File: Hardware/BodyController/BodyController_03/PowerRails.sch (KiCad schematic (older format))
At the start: 44 parts, among them Q10 NX1029X,115, Q11 NX1029X,115, U18 TLV70033DDC, U19 TLV70033DDC, U20 LMR140x0

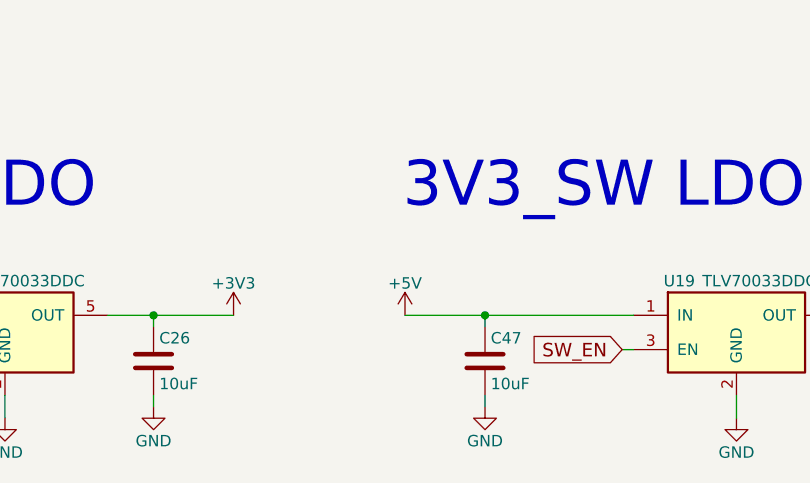
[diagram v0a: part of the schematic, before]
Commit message: Updated layout, cleaned up directory, and modified BOM
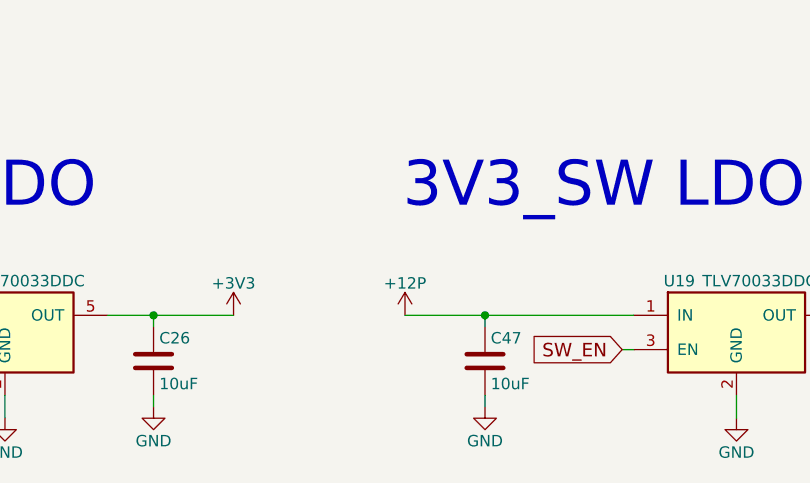
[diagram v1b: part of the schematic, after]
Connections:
- net +12P: now also C47.1, U19.1 (IN)
- net +5V: no longer C47.1, U19.1 (IN)
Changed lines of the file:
@@
 EESchema Schematic File Version 2
+LIBS:BodyController_03-rescue
 LIBS:power
 LIBS:device
@@
 LIBS:contrib
 LIBS:valves
-LIBS:HSD
-LIBS:micros
-LIBS:ICs
-LIBS:Connectors
 LIBS:BodyController_03-cache
 EELAYER 25 0
@@
 F 3 "http://www.ti.com/lit/ds/slvsa00e/slvsa00e.pdf" H 5550 6950 50  0001 C CNN
 	1    5550 6950
-	1    0    0    -1
-$EndComp
-$Comp
-L +5V #PWR0214
-U 1 1 59A6B09C
-P 4100 6900
-F 0 "#PWR0214" H 4100 6750 50  0001 C CNN
-F 1 "+5V" H 4100 7040 50  0000 C CNN
-F 2 "" H 4100 6900 50  0001 C CNN
-F 3 "" H 4100 6900 50  0001 C CNN
-	1    4100 6900
 	1    0    0    -1
 $EndComp
@@
 Connection ~ 3500 4000
 Connection ~ 4850 4900
+$Comp
+L +12P #PWR?
+U 1 1 59ED23A1
+P 4100 6900
+F 0 "#PWR?" H 4100 6750 50  0001 C CNN
+F 1 "+12P" H 4100 7040 50  0000 C CNN
+F 2 "" H 4100 6900 50  0001 C CNN
+F 3 "" H 4100 6900 50  0001 C CNN
+	1    4100 6900
+	1    0    0    -1
+$EndComp
 $EndSCHEMATC

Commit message: started serious layout
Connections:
- net +12P: no longer C47.1, U19.1 (IN)
- net +12V: now also C47.1, U19.1 (IN)
- net 12P_MONITOR renamed 12P_MONITOR_AI

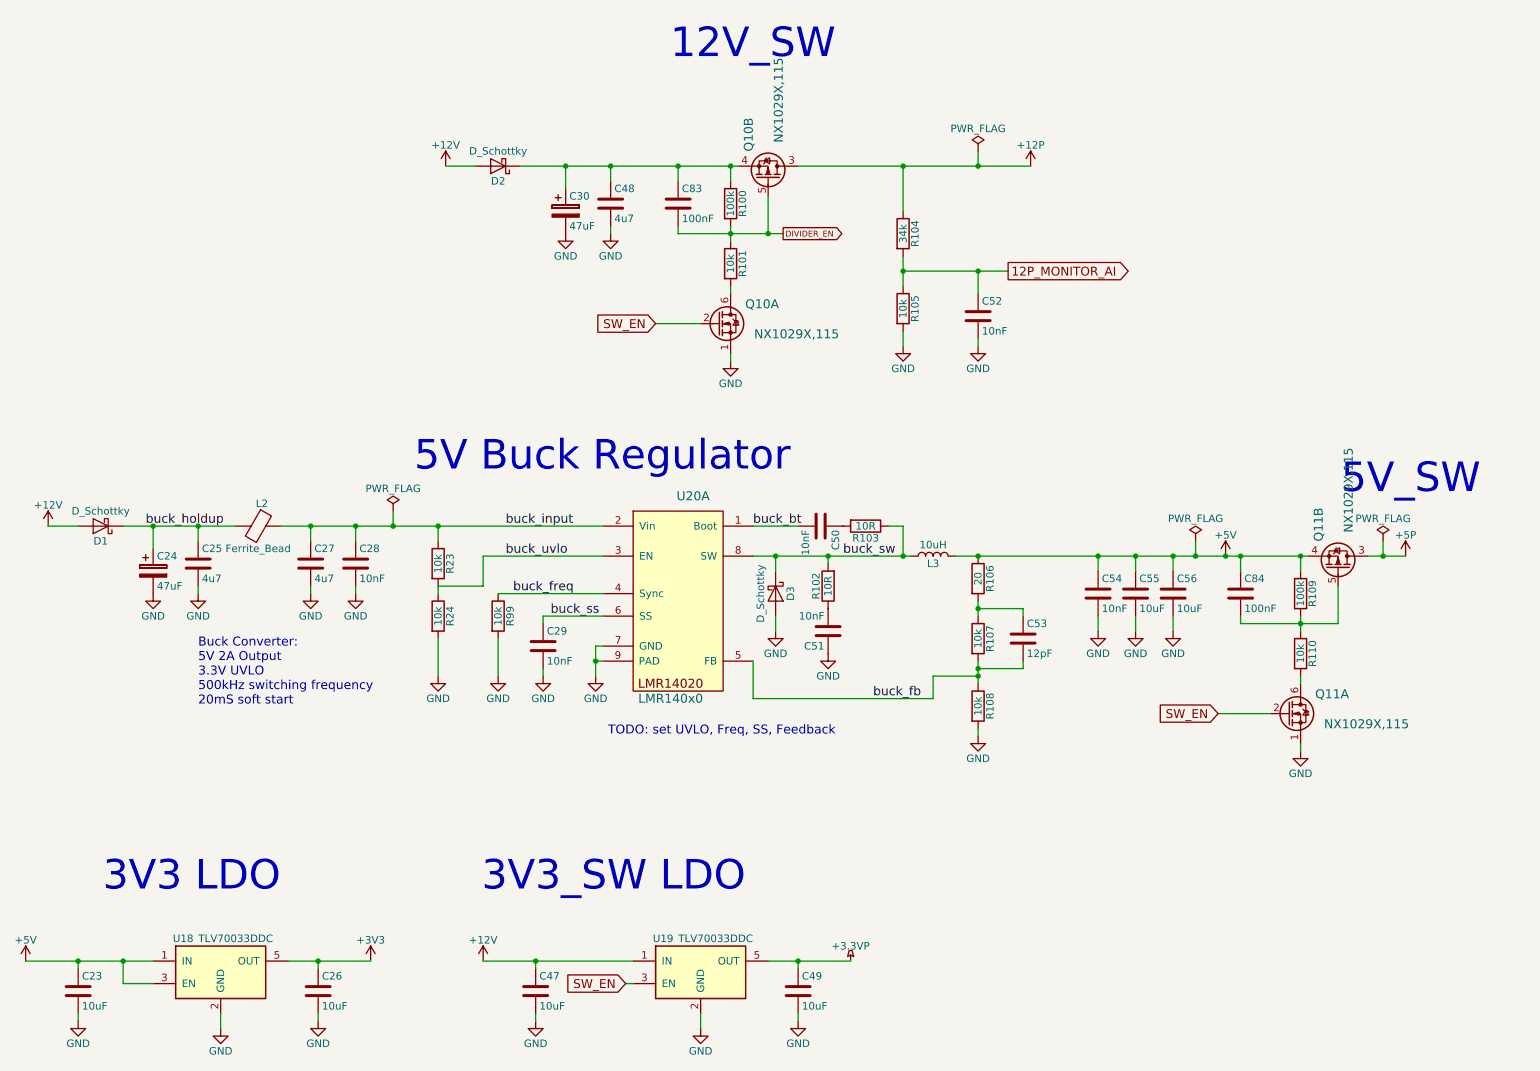
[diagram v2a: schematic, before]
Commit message: Body Controller Layout Done
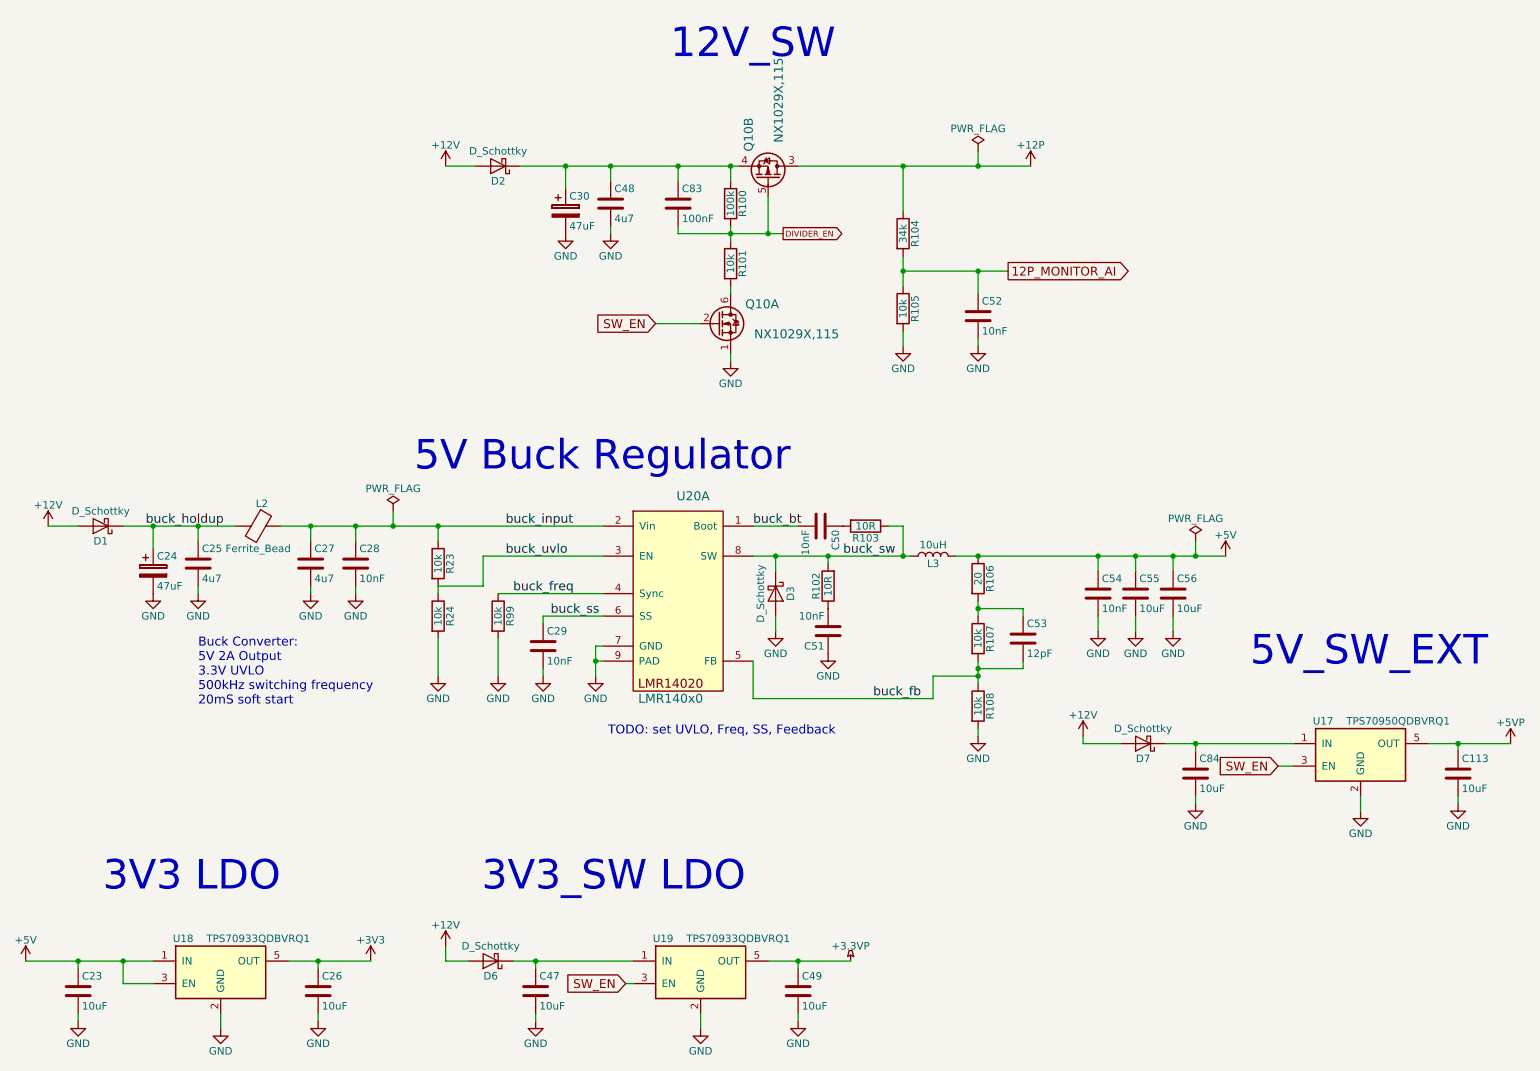
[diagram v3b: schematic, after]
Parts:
- removed Q11: NX1029X,115, TO_SOT_Packages_SMD:SOT-666, symbol NX1029X,115
- removed R109: 100k, Resistors_SMD:R_0603, symbol R
- removed R110: 10k, Resistors_SMD:R_0603, symbol R
- added C113: 10uF, Capacitors_SMD:C_1206, symbol C
- added D6, D7: D_Schottky, Diodes_SMD:D_SOD-123, symbol D_Schottky
- added U17: TPS70950QDBVRQ1, TO_SOT_Packages_SMD:SOT-23-5, symbol TLV70033DDC
- C84: value 100nF -> 10uF; footprint Capacitors_SMD:C_0603 -> Capacitors_SMD:C_1206; PartNumber CGA3E2X7R1H104K080AA -> CGA5L1X7R1E106M160AC
- U18, U19: value TLV70033DDC -> TPS70933QDBVRQ1; PartNumber (none) -> TPS70933QDBVRQ1
- U20: footprint Housings_SOIC:Diodes_PSOP-8 -> Housings_SOIC:HTSOP-8-1EP_3.9x4.9mm_Pitch1.27mm_ThermalVias
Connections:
- net +12V: now also D6.2 (A), D7.2 (A); no longer C47.1, U19.1 (IN)
- net +5V: no longer C84.1
- net GND: now also C84.2, C113.2, U17.2 (GND)
- net SW_EN: now also U17.3 (EN)
- new net: C47.1, D6.1 (K), U19.1 (IN)
- new net: C84.1, D7.1 (K), U17.1 (IN)
- new net +5VP: C113.1, U17.5 (OUT)
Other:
- note added: "5V_SW_EXT"
- note removed: "5V_SW"

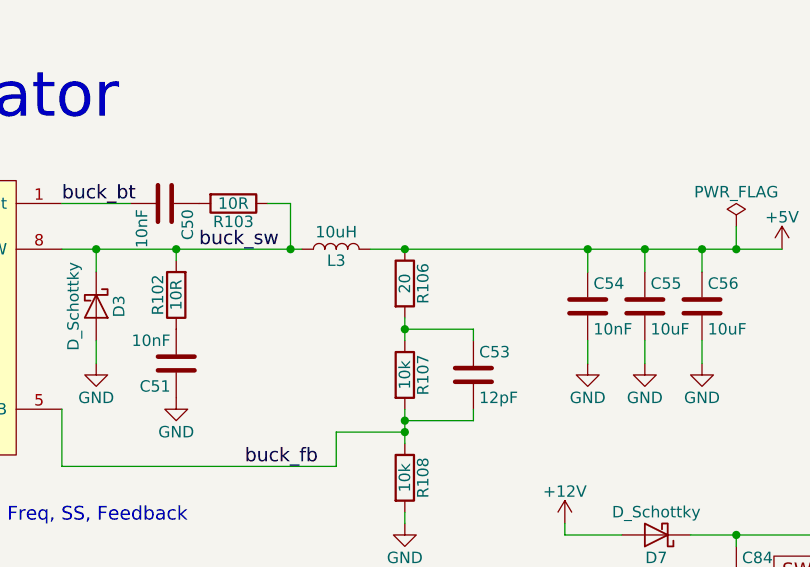
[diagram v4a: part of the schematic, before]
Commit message: Added resistor values via BOM importer. Changed layout file to add large CAN resistors and buffer to 1.65V Reference
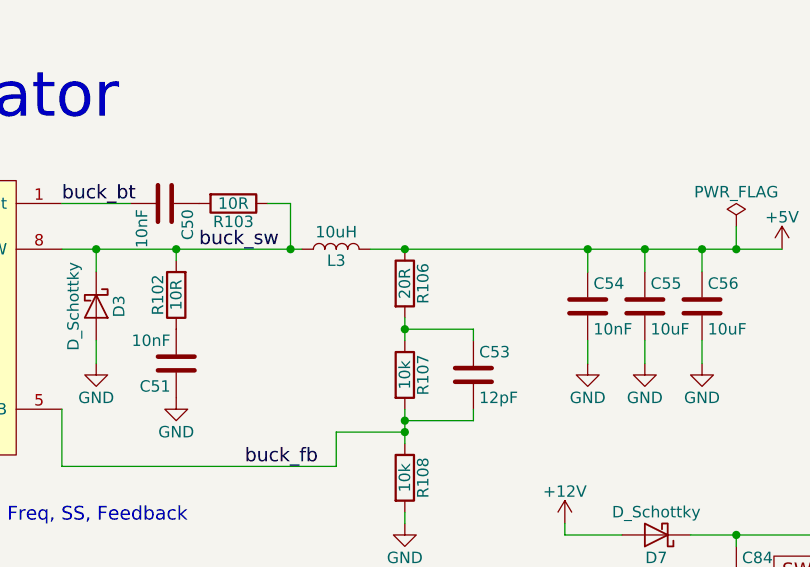
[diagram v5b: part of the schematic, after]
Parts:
- R100: PartNumber (none) -> AC0603FR-07100KL
- R101, R105, R107, R108, R23, R24, R99: PartNumber (none) -> AC0603FR-0710KL
- R102, R103: PartNumber (none) -> AC0603FR-0710RL
- R104: PartNumber (none) -> ERJ-3EKF3402V
- R106: value 20 -> 20R; PartNumber (none) -> AC0603FR-0720RL
